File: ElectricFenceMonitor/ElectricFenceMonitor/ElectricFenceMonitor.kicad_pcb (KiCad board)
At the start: 2 copper layers, 101.6 x 58.4 mm, 30 parts, among them J1 Fence wire, J2 Fence ground, J3 Power, J4 Programming, Q1 BC548, U1 Ra01_Breakout_Module, U2 PICAXE-14M2

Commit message: Water baby layout, electric fence simulations
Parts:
- moved U1 2.54 mm to (175.3, 78.7)
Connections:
- C2 pad 1: +3.3V -> Net-(Q1-C)
- Q1 pad 1: +3.3V -> Net-(Q1-C)
- R5 pad 1: +3.3V -> Net-(Q1-C)
- R8 pad 1: +3.3V -> Net-(Q1-C)
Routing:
- net +3.3V: track 115.6 -> 67.7 mm, vias 6 -> 4
- net Net-(Q1-C): track 0.00 -> 17.8 mm
- net GND: track 222.8 -> 226.4 mm
- net Net-(U1-SCK): track 12.7 -> 15.2 mm
- net Net-(U1-RST): track 12.7 -> 15.2 mm
- net Net-(U1-NSS): track 53.3 -> 50.8 mm
- net Net-(U1-MISO): track 12.7 -> 15.2 mm
- net Net-(U1-DIO0): track 27.9 -> 30.5 mm
- net Net-(U1-MOSI): track 38.1 -> 36.5 mm

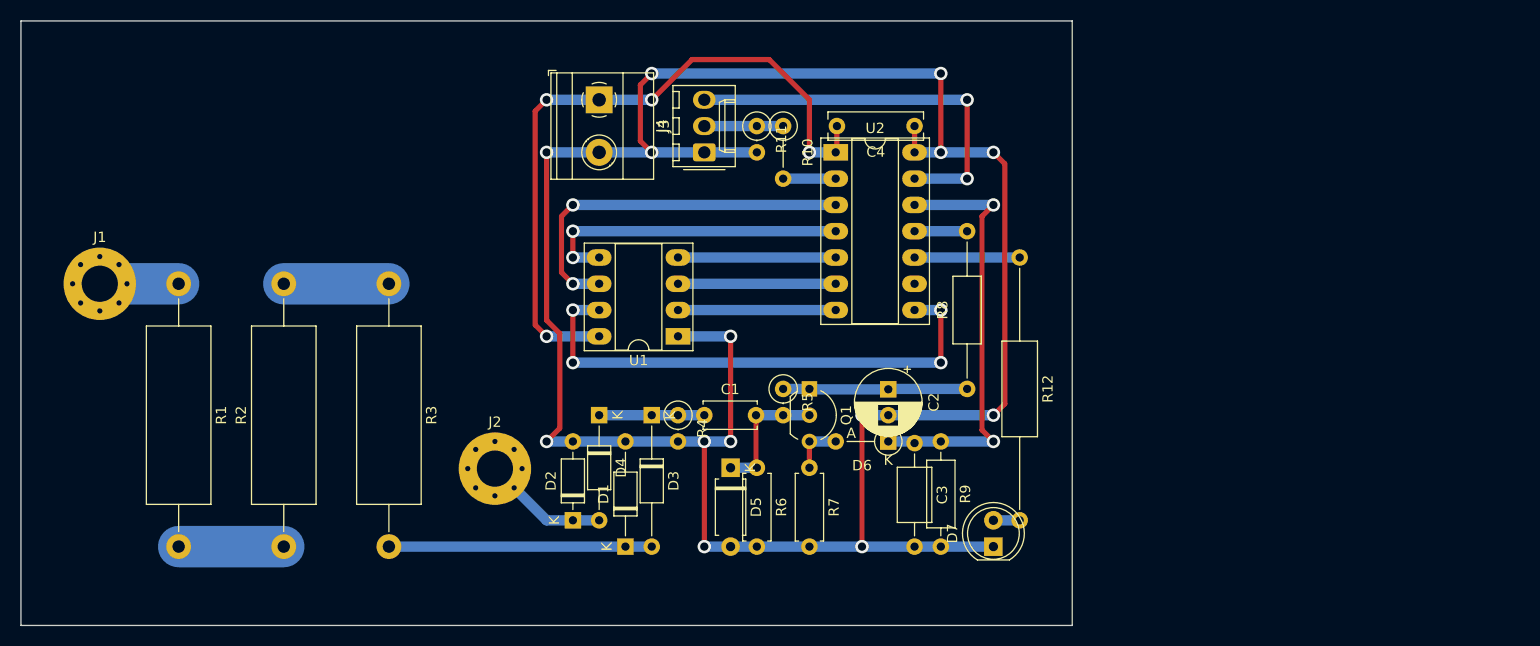
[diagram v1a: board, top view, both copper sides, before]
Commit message: Electric fence monitor schematic updated, layout redone
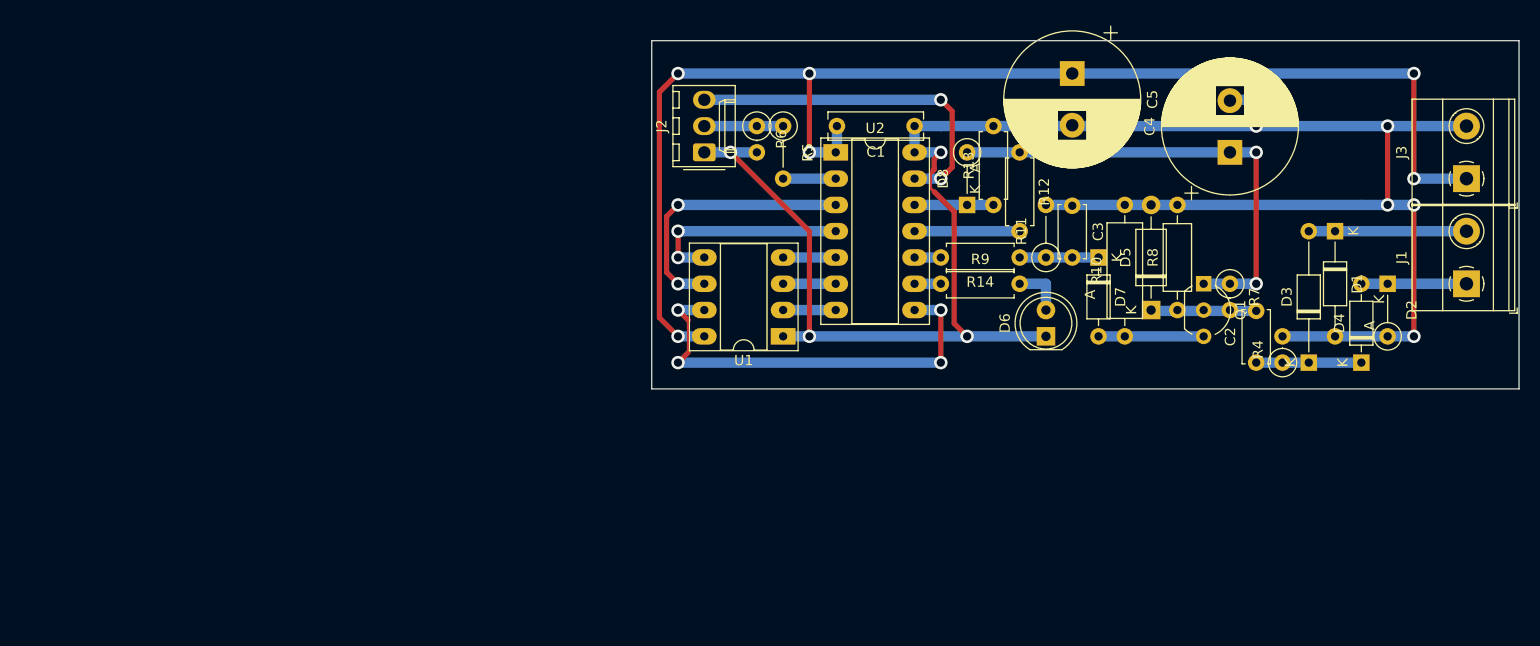
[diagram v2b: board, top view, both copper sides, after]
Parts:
- removed the C2 at (195.6, 83.9)
- removed the J2 at (157.6, 91.5)
- removed R1, R2, R3: 8.2Meg, Resistor_THT:R_Axial_DIN0617_L17.0mm_D6.0mm_P25.40mm_Horizontal
- removed the R8 at (203.2, 83.8)
- added C4: 10u, Capacitor_THT:CP_Radial_D13.0mm_P5.00mm, F.Cu at (228.6, 61.0)
- added C5: 100u, Capacitor_THT:CP_Radial_D13.0mm_P5.00mm, F.Cu at (213.4, 53.3)
- added D8: 1N4148, Diode_THT:D_DO-35_SOD27_P5.08mm_Vertical_KathodeUp, F.Cu at (203.2, 66.0)
- added R12: 180, Resistor_THT:R_Axial_DIN0207_L6.3mm_D2.5mm_P7.62mm_Horizontal, F.Cu at (208.3, 61.0)
- added R13: 2.2k, Resistor_THT:R_Axial_DIN0207_L6.3mm_D2.5mm_P7.62mm_Horizontal, F.Cu at (205.7, 66.0)
- added R14: 1k, Resistor_THT:R_Axial_DIN0207_L6.3mm_D2.5mm_P7.62mm_Horizontal, F.Cu at (208.3, 71.1)
- C3: value 2.2u -> 0.47u; footprint Capacitor_THT:C_Axial_L5.1mm_D3.1mm_P10.00mm_Horizontal -> Capacitor_THT:C_Disc_D5.0mm_W2.5mm_P5.00mm
- D2: footprint Diode_THT:D_DO-35_SOD27_P7.62mm_Horizontal -> Diode_THT:D_DO-35_SOD27_P5.08mm_Vertical_KathodeUp
- D4: footprint Diode_THT:D_DO-35_SOD27_P10.16mm_Horizontal -> Diode_THT:D_DO-35_SOD27_P7.62mm_Horizontal
- D5: footprint Diode_THT:D_A-405_P7.62mm_Horizontal -> Diode_THT:D_A-405_P10.16mm_Horizontal
- D7: renamed from D6; footprint Diode_THT:D_DO-35_SOD27_P5.08mm_Vertical_AnodeUp -> Diode_THT:D_DO-35_SOD27_P7.62mm_Horizontal
- J1: value Fence wire -> Fence; footprint MountingHole:MountingHole_3.5mm_Pad_Via -> TerminalBlock_Phoenix:TerminalBlock_Phoenix_MKDS-1,5-2-5.08_1x02_P5.08mm_Horizontal
- R10: renamed from R7; value 10k -> 33k; footprint Resistor_THT:R_Axial_DIN0207_L6.3mm_D2.5mm_P7.62mm_Horizontal -> Resistor_THT:R_Axial_DIN0309_L9.0mm_D3.2mm_P12.70mm_Horizontal
- R11: renamed from R9; value 1Meg -> 10Meg; footprint Resistor_THT:R_Axial_DIN0207_L6.3mm_D2.5mm_P10.16mm_Horizontal -> Resistor_THT:R_Axial_DIN0207_L6.3mm_D2.5mm_P5.08mm_Vertical
- R4: value 4.7k -> 120
- R7: renamed from R5; value 100k -> 120k
- R8: renamed from R6; value 100k -> 82k; footprint Resistor_THT:R_Axial_DIN0207_L6.3mm_D2.5mm_P7.62mm_Horizontal -> Resistor_THT:R_Axial_DIN0207_L6.3mm_D2.5mm_P10.16mm_Horizontal
- R9: renamed from R12; value 470 -> 220; footprint Resistor_THT:R_Axial_DIN0309_L9.0mm_D3.2mm_P25.40mm_Horizontal -> Resistor_THT:R_Axial_DIN0207_L6.3mm_D2.5mm_P7.62mm_Horizontal
- moved J1 132.1 mm to (251.5, 73.7), turned to 90 degrees
- moved J3 84.2 mm to (251.5, 63.5), turned to 90 degrees
- moved D2 82.0 mm to (243.8, 73.7), turned to -90 degrees
- moved D1 75.0 mm to (238.8, 68.6), turned to -90 degrees
- moved D4 73.8 mm to (241.3, 81.3), turned to 90 degrees
- moved D3 63.7 mm to (236.2, 81.3), turned to 90 degrees
- moved R4 58.6 mm to (233.7, 81.3), turned to 90 degrees
- moved C2 53.6 mm to (231.1, 81.3), turned to 90 degrees
- moved R7 44.4 mm to (228.6, 73.7)
- moved R8 43.4 mm to (223.5, 76.2), turned to 90 degrees
- moved D5 43.4 mm to (221.0, 76.2), turned to 90 degrees
- moved Q1 39.4 mm to (226.1, 73.7)
- moved R10 33.0 mm to (218.4, 78.7), turned to 90 degrees
- moved C3 27.5 mm to (213.4, 66.1)
- moved D7 27.0 mm to (215.9, 71.1), turned to -90 degrees
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- renumbered C4 to C1, C1 to C2, D7 to D6, J4 to J2, R10 to R5, R11 to R6
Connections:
- C3 pad 1: Fence peak -> GND
- C3 pad 2: GND -> Net-(D7-K)
- D7 pad 1: Fence peak -> Net-(D7-K)
- J1 pad 1: Net-(J1-Pad1) -> Net-(D2-K)
- Q1 pad 1: Net-(Q1-C) -> Fence power
- R11 pad 1: Fence peak -> Net-(D7-K)
- R7 pad 1: Net-(Q1-C) -> Fence power
- R9 pad 1: Net-(U2-B.3) -> Net-(U2-B.4)
- U2 pad 10: Net-(U2-B.3) -> Fence peak
- U2 pad 11: Fence power -> Fence switched
- U2 pad 12: Fence peak -> ADC reference
- U2 pad 9: unconnected-(U2-B.4-Pad9) -> Net-(U2-B.4)
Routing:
- net +3.3V: track 67.7 -> 128.7 mm, vias 4 -> 6
- net Fence power: track 5.08 -> 45.7 mm, vias 0 -> 2
- net Fence peak: track 41.6 -> 2.54 mm, vias 2 -> 0
- net GND: track 226.4 -> 203.2 mm, vias 14 -> 10
- net Net-(Q1-C): track 17.8 -> 0.00 mm
- net Net-(U2-B.3): track 10.2 -> 0.00 mm
- net Net-(U1-SCK): track 15.2 -> 5.08 mm
- net Net-(U1-RST): track 15.2 -> 5.08 mm
- net Net-(U1-MISO): track 15.2 -> 5.08 mm
- net Net-(R2-Pad2): track 10.2 -> 0.00 mm
- net Net-(R1-Pad2): track 10.2 -> 0.00 mm
- net Net-(D1-K): track 25.4 -> 15.2 mm
- net Fence switched: track 0.00 -> 10.2 mm
- net Net-(U1-DIO0): track 30.5 -> 20.3 mm
- net Net-(U1-MOSI): track 36.5 -> 26.3 mm
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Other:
- board size 101.6 x 58.4 mm -> 83.8 x 33.7 mm
